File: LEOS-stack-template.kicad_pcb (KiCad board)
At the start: 2 copper layers, 100 x 100 mm, 19 parts, among them J1 MicroFit_1x4, J2 MicroFit_1x4, U1 MCP2562FD, U2 MCP2518FD, Y1 40 MHz

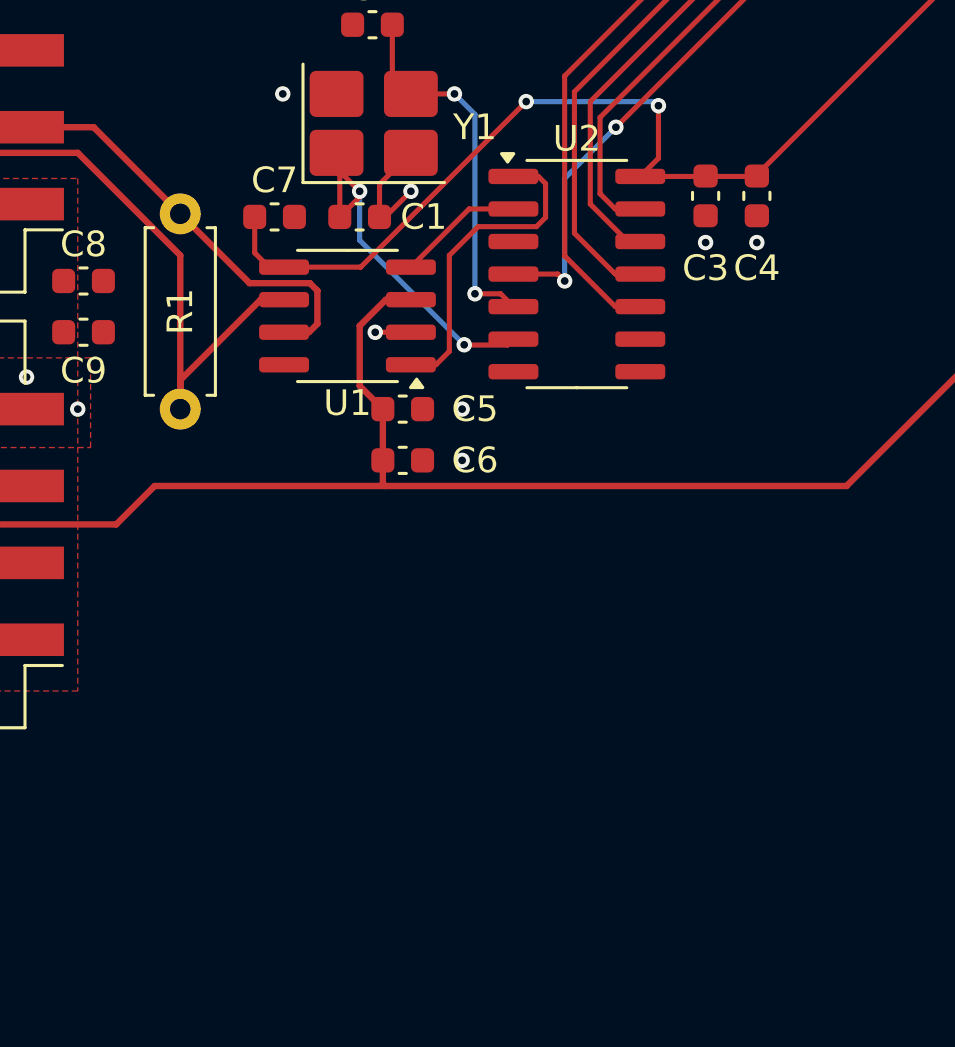
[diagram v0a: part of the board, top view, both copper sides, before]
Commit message: Added the 12-5V buck converter to the schematic
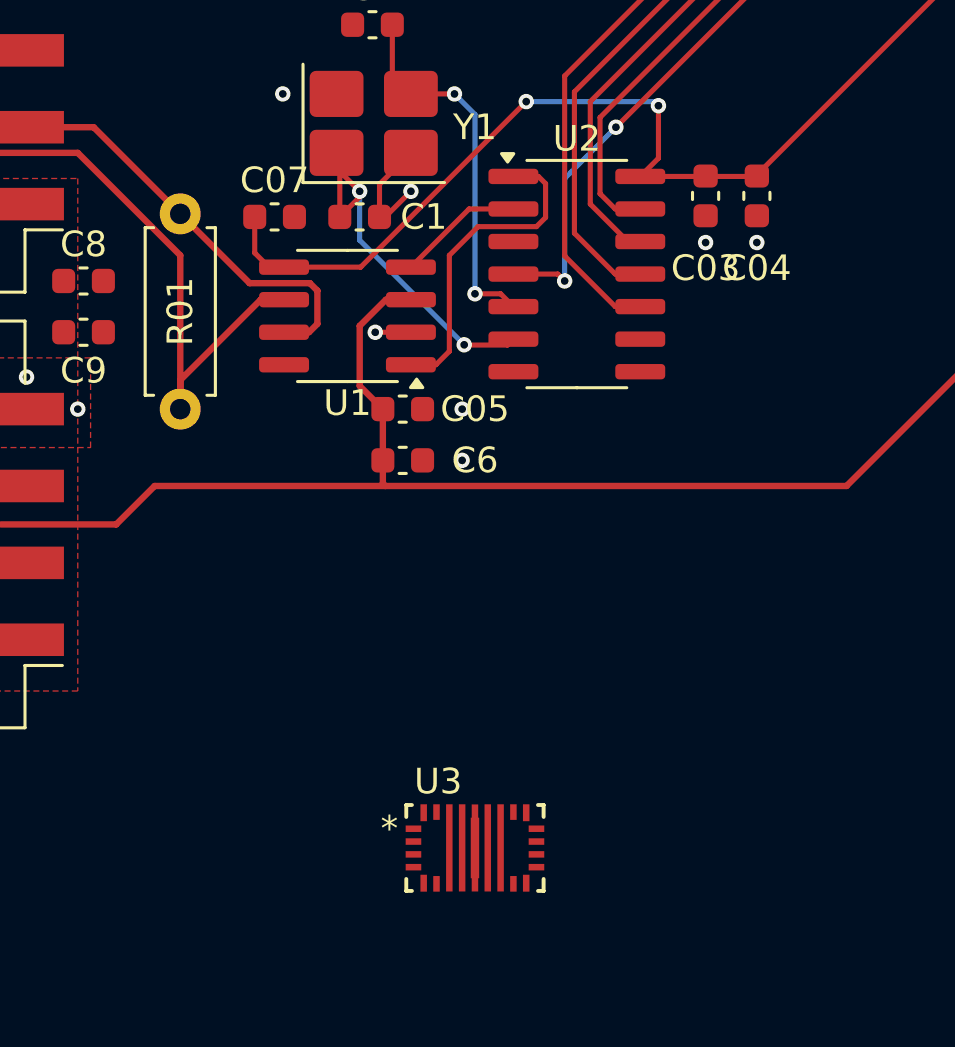
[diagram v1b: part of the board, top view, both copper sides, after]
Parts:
- added U3: TPS55287, LEOS:VQFN21_RYQ_TEX, F.Cu at (128.5, 93.1)
- C03: renamed from C3; value 0.1uF -> 4.7uF
- C04: renamed from C4; value 1uF -> 0.1uF
- C07: renamed from C7; value 0.1uF -> 36.5nF
- R01: renamed from R1; value 120R -> 9.3k
- renumbered C5 to C05
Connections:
- C03 pad 1: VDD -> Net-(U3-VCC)
- C03 pad 2: GND -> GNDA
- C04 pad 1: VDD -> Net-(U3-SW1)
- C04 pad 2: GND -> Net-(U3-BOOT1)
- C05 pad 1: +5V -> Net-(U3-SW2)
- C05 pad 2: GND -> Net-(U3-BOOT2)
- C07 pad 1: VDD -> Net-(U3-COMP)
- C07 pad 2: GND -> Net-(C06-Pad2)
- R01 pad 1: /CAN- -> Net-(U3-FSW)
- R01 pad 2: /CAN+ -> GNDA

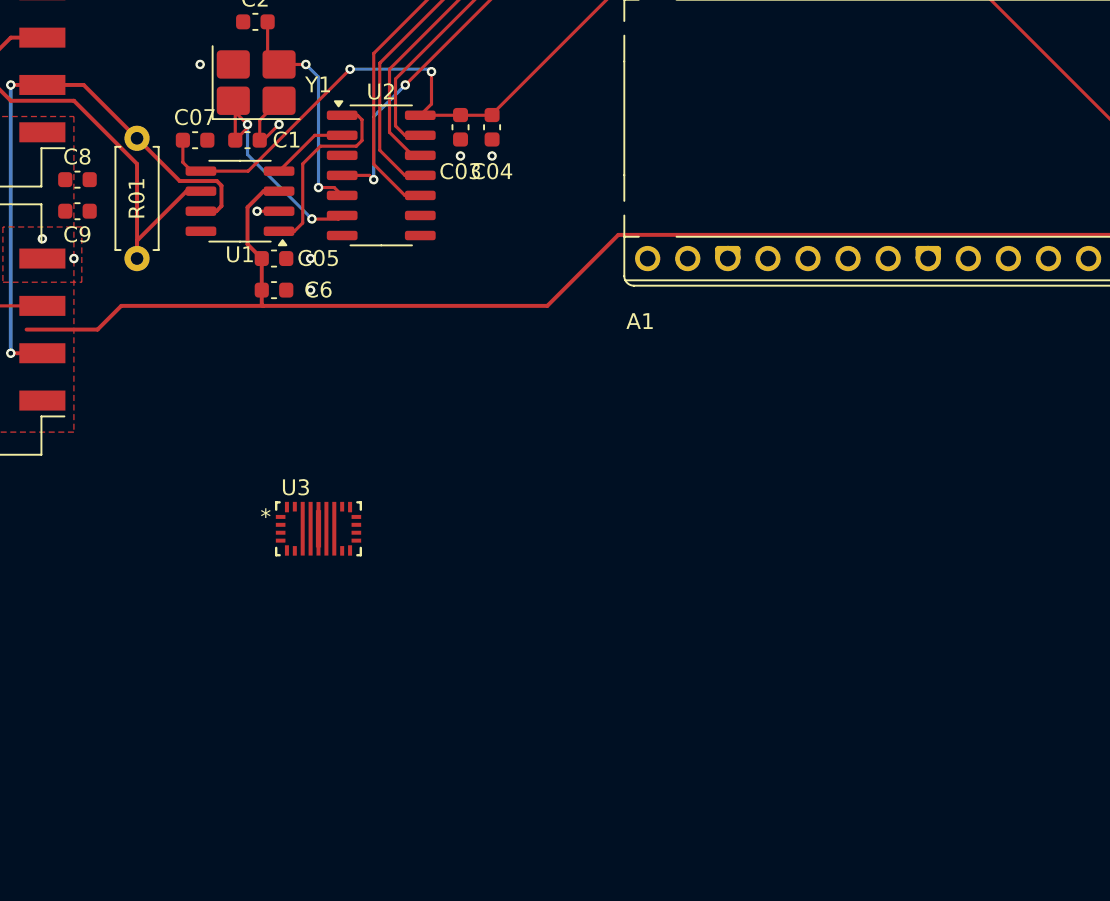
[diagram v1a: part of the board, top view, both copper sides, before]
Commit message: updates to schematic and added footprints
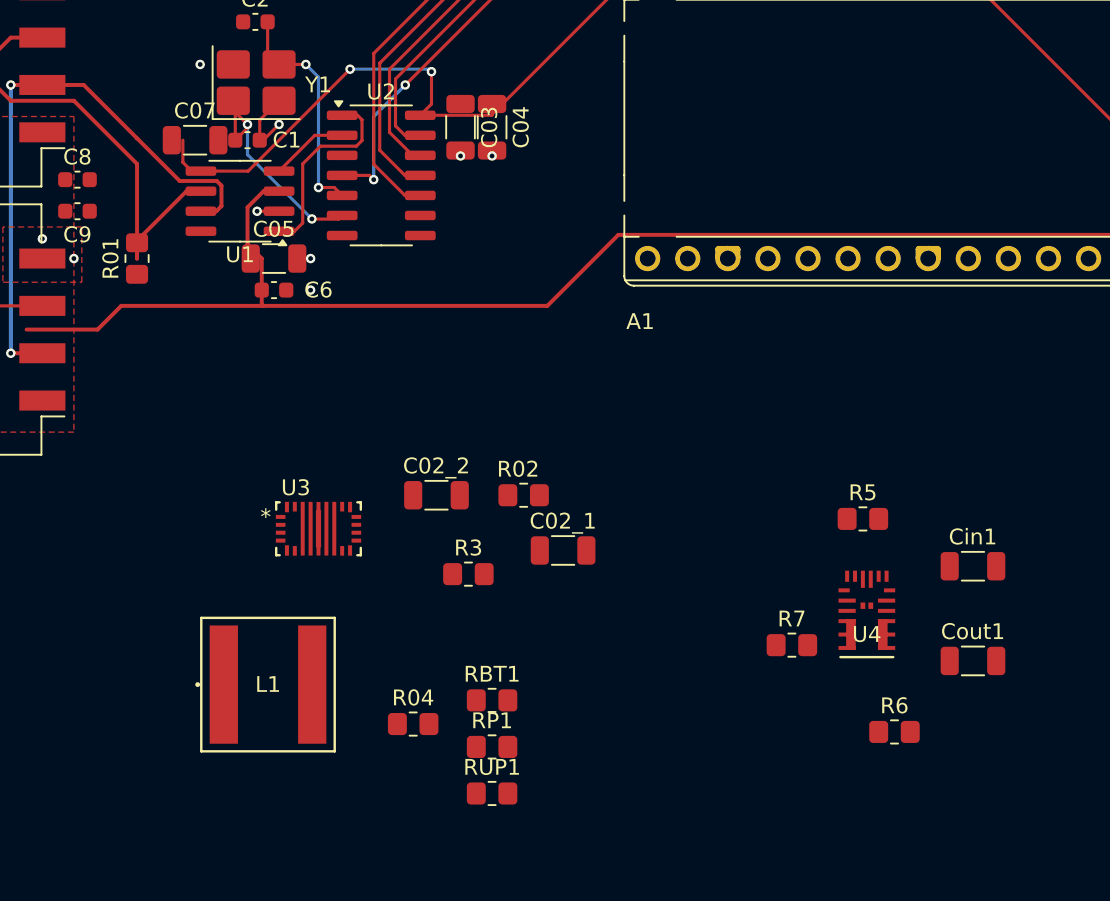
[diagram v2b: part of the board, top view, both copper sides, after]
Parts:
- added C02_1: 22uF, Capacitor_SMD:C_1206_3216Metric, F.Cu at (144.0, 94.5)
- added C02_2: 22uF, Capacitor_SMD:C_1206_3216Metric, F.Cu at (136.0, 91.0)
- added Cin1: 10uF, Capacitor_SMD:C_1206_3216Metric, F.Cu at (170.0, 95.5)
- added Cout1: 22uF, Capacitor_SMD:C_1206_3216Metric, F.Cu at (170.0, 101.5)
- added L1: 10uH, LEOS:IND_TAIYO_NRS8030_TAY, F.Cu at (125.3, 103.0)
- added R02: 20k, Resistor_SMD:R_0805_2012Metric_Pad1.20x1.40mm_HandSolder, F.Cu at (141.5, 91.0)
- added R04: 16m, Resistor_SMD:R_0805_2012Metric_Pad1.20x1.40mm_HandSolder, F.Cu at (134.5, 105.5)
- added R3: 7.23k, Resistor_SMD:R_0805_2012Metric_Pad1.20x1.40mm_HandSolder, F.Cu at (138.0, 96.0)
- added R5: 100k, Resistor_SMD:R_0805_2012Metric_Pad1.20x1.40mm_HandSolder, F.Cu at (163.0, 92.5)
- added R6: 100k, Resistor_SMD:R_0805_2012Metric_Pad1.20x1.40mm_HandSolder, F.Cu at (165.0, 106.0)
- added R7: 19.1k, Resistor_SMD:R_0805_2012Metric_Pad1.20x1.40mm_HandSolder, F.Cu at (158.5, 100.5)
- added RBT1: 11.1k, Resistor_SMD:R_0805_2012Metric_Pad1.20x1.40mm_HandSolder, F.Cu at (139.5, 104.0)
- added RP1: 10k, Resistor_SMD:R_0805_2012Metric_Pad1.20x1.40mm_HandSolder, F.Cu at (139.5, 107.0)
- added RUP1: 100k, Resistor_SMD:R_0805_2012Metric_Pad1.20x1.40mm_HandSolder, F.Cu at (139.5, 109.9)
- added U4: MPM3620A, LEOS:IC18_MPM3620AGQV-Z_MNP, F.Cu at (163.2, 98.6)
- C03, C04, C05, C07: footprint Capacitor_SMD:C_0603_1608Metric -> Capacitor_SMD:C_1206_3216Metric
- R01: footprint Resistor_THT:R_Axial_DIN0207_L6.3mm_D2.5mm_P7.62mm_Horizontal -> Resistor_SMD:R_0805_2012Metric_Pad1.20x1.40mm_HandSolder

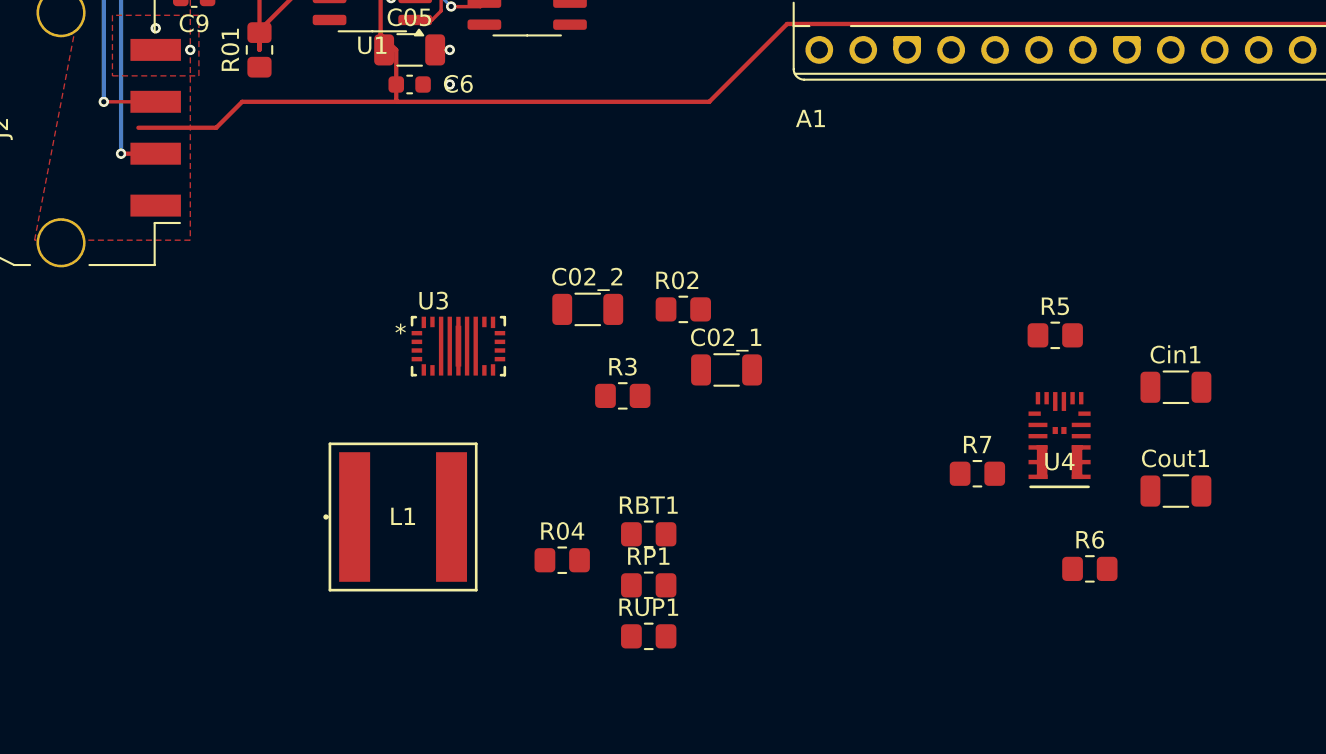
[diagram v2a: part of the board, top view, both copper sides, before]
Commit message: routed the 12-5V buck converter
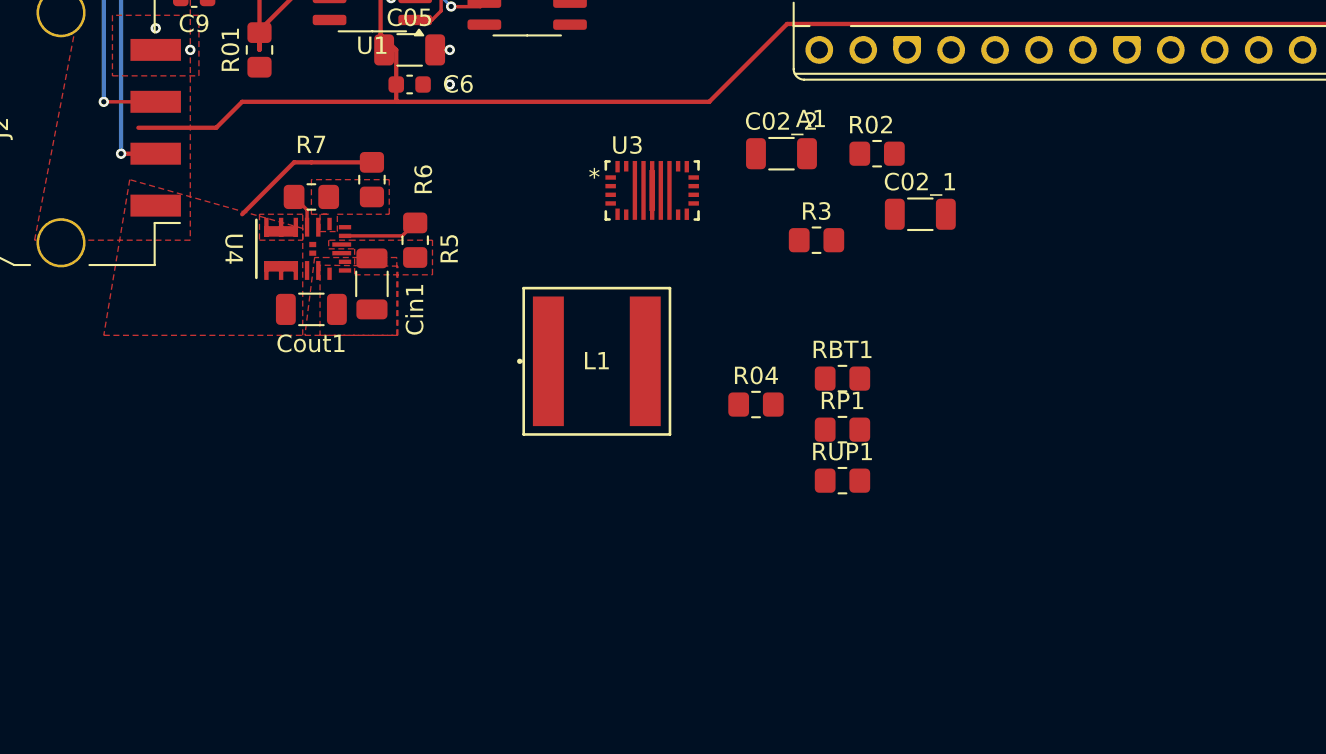
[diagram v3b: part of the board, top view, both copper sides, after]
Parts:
- moved Cout1 51.1 mm to (120.0, 91.0)
- moved R6 47.2 mm to (123.5, 83.5), turned to -90 degrees
- moved Cin1 46.9 mm to (123.5, 89.5), turned to -90 degrees
- moved U4 45.1 mm to (119.5, 87.5), turned to -90 degrees
- moved R7 41.7 mm to (120.0, 84.5), turned to 180 degrees
- moved R5 37.4 mm to (126.0, 87.0), turned to 90 degrees
- moved C02_2 14.4 mm to (147.2, 82.0)
- moved U3 14.4 mm to (139.7, 84.1)
- moved L1 14.4 mm to (136.5, 94.0)
- moved C02_1 14.4 mm to (155.2, 85.5)
- moved R02 14.4 mm to (152.7, 82.0)
- moved R04 14.4 mm to (145.7, 96.5)
- moved R3 14.4 mm to (149.2, 87.0)
- moved RBT1 14.4 mm to (150.7, 95.0)
- moved RP1 14.4 mm to (150.7, 98.0)
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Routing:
- net +5V: track 101.8 -> 110.6 mm
- net Net-(U4-EN): track 0.00 -> 4.37 mm
- net GNDA2: track 0.00 -> 2.06 mm
- added copper zone on F.Cu, net /FB
- added copper zone on F.Cu, net /SW
- added copper zone on F.Cu, net /VIN
